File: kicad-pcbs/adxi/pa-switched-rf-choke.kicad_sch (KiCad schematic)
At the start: 51 parts

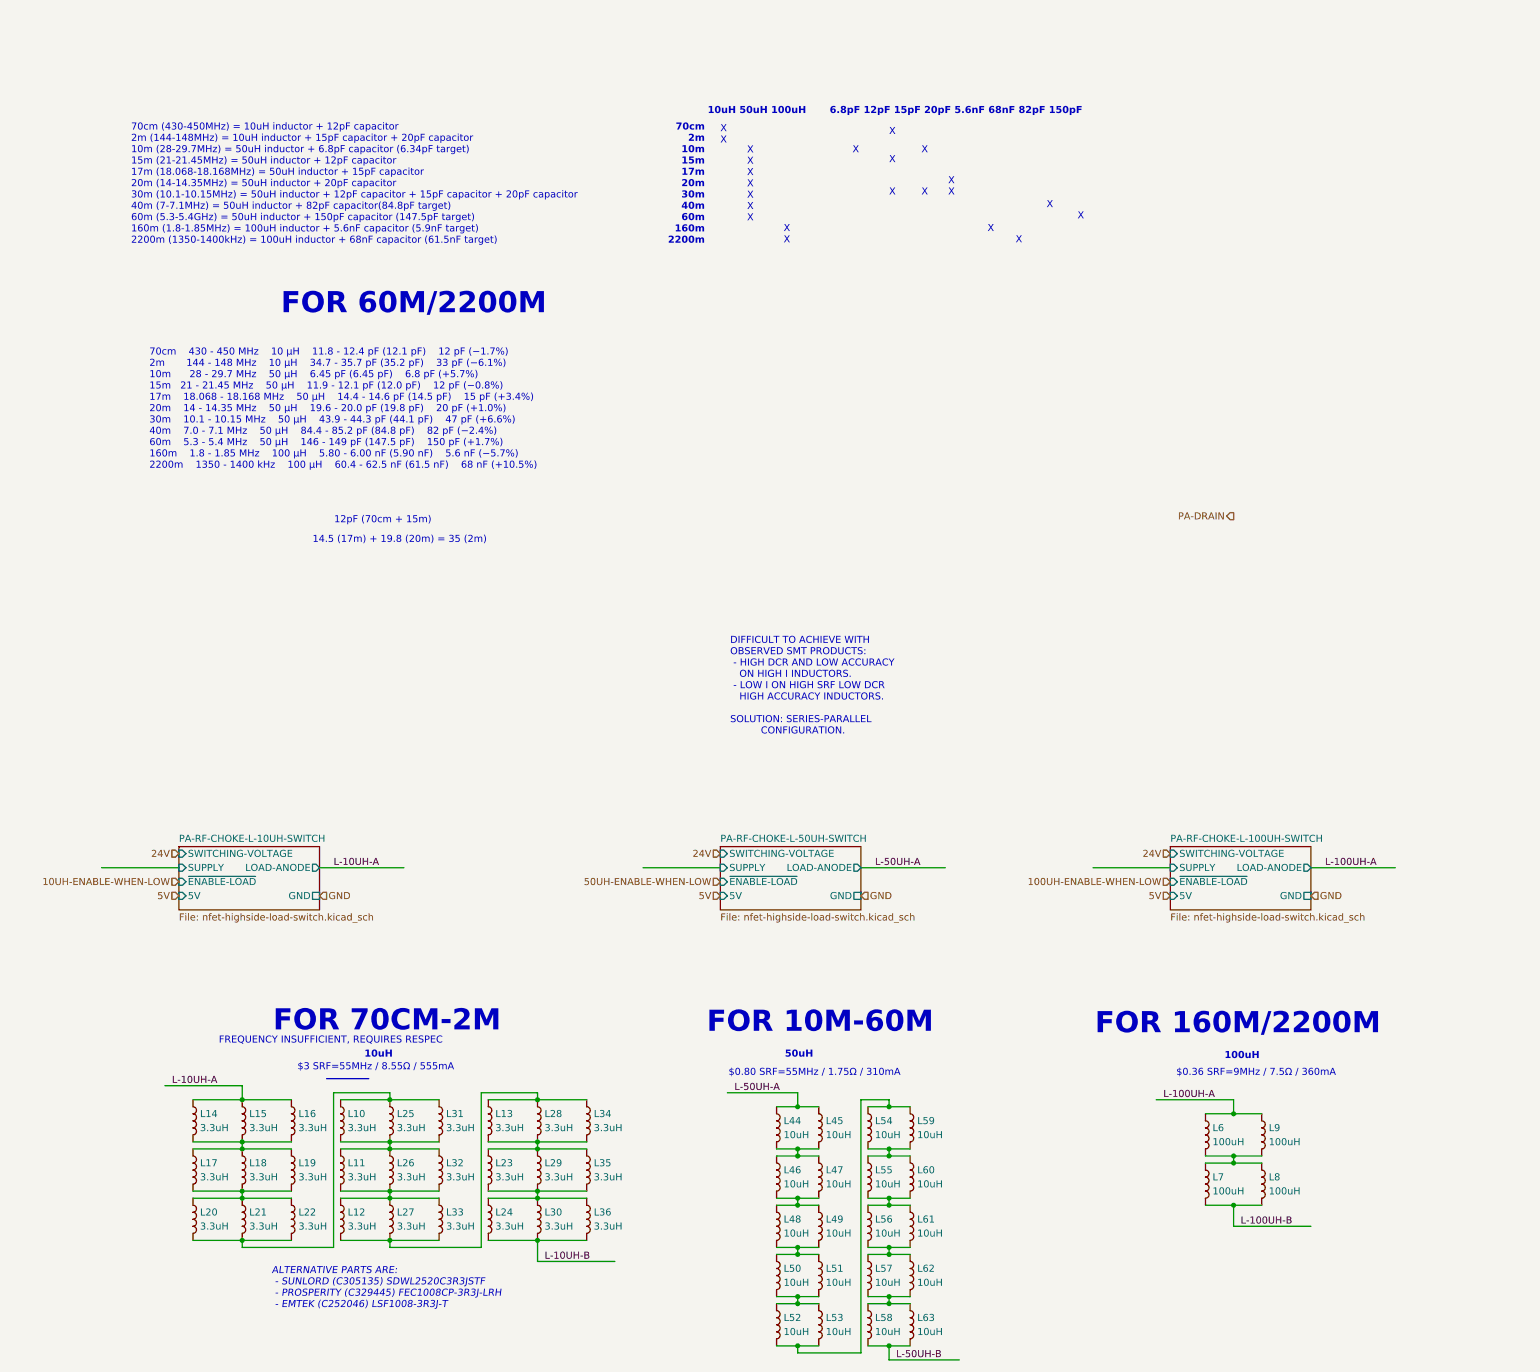
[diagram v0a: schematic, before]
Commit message: Working inductor array
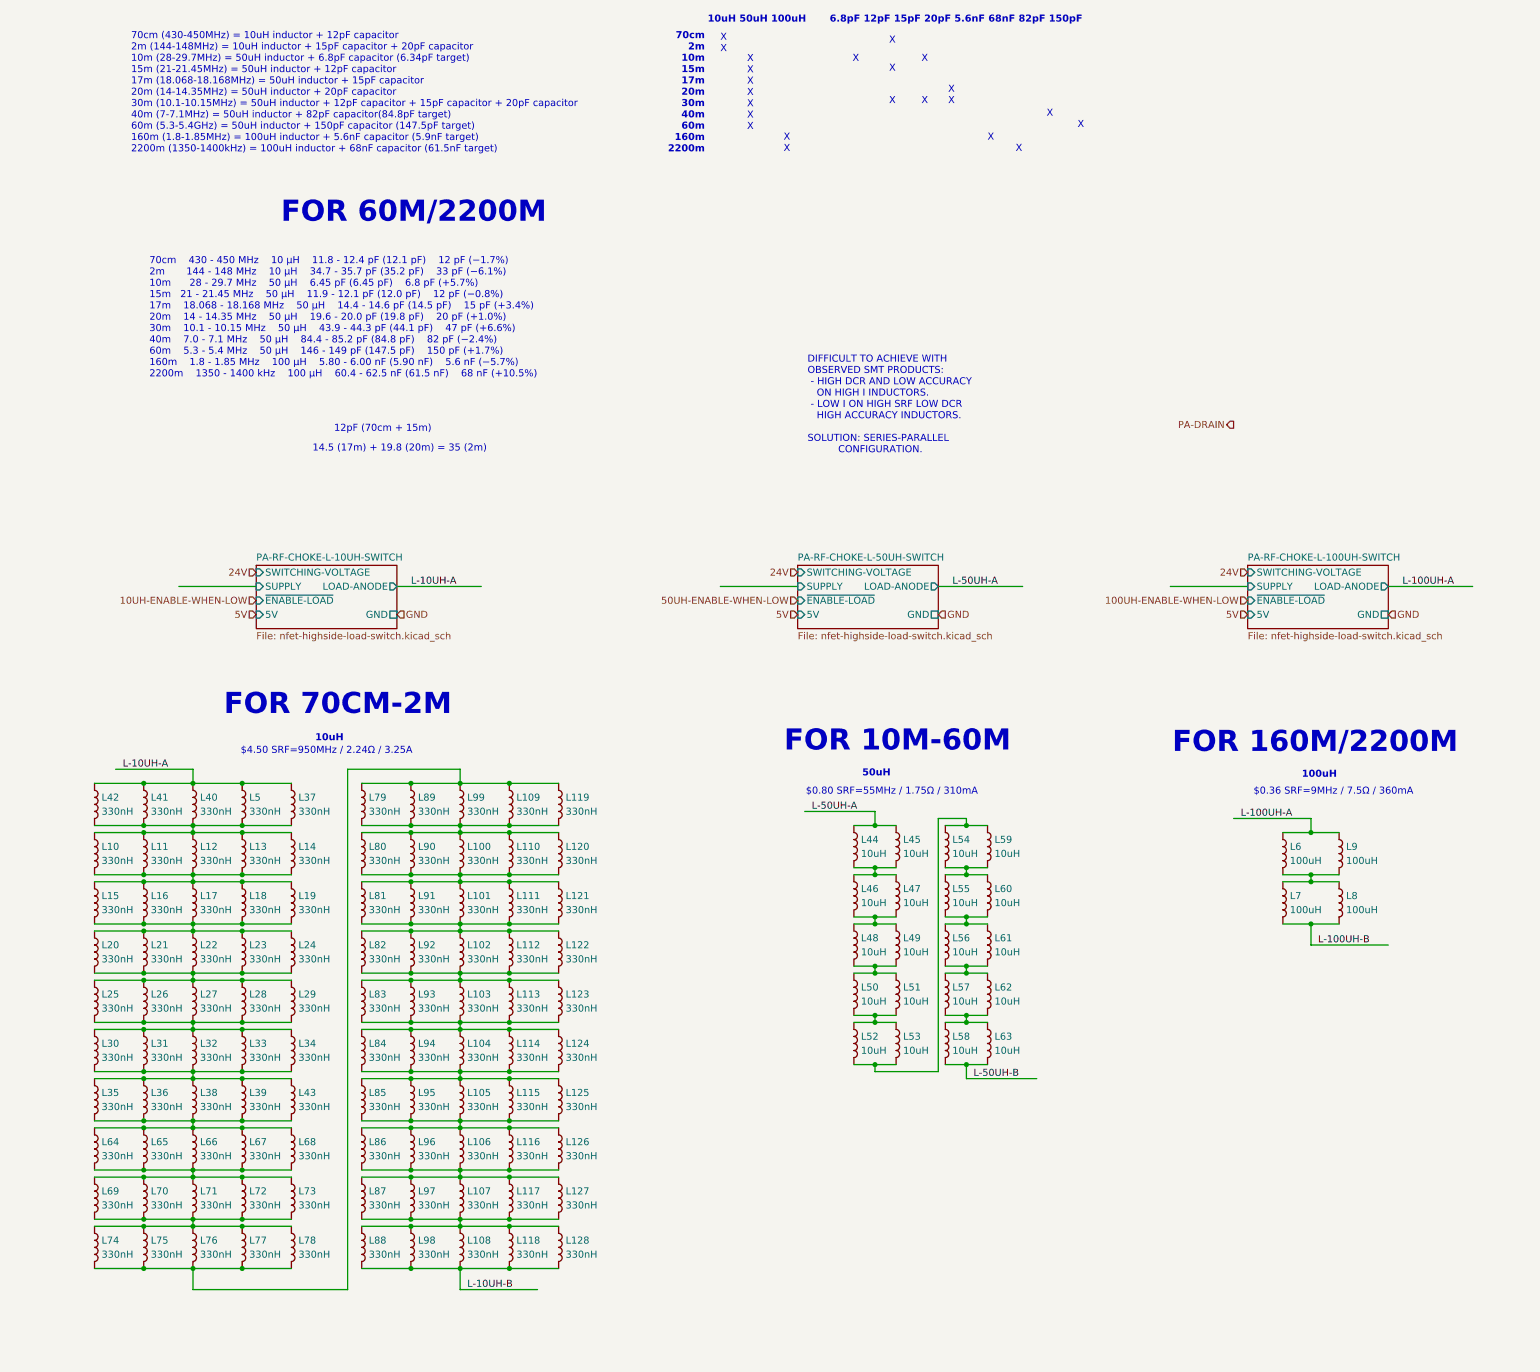
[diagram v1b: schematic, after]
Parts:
- added L100, L101, L102, L103, L104, L105, L106, L107, L108, L109, L110, L111, L112, L113, L114, L115, L116, L117, L118, L119, L120, L121, L122, L123, L124, L125, L126, L127, L128, L37, L38, L39, L40, L41, L42, L43, L5, L64, L65, L66, L67, L68, L69, L70, L71, L72, L73, L74, L75, L76, L77, L78, L79, L80, L81, L82, L83, L84, L85, L86, L87, L88, L89, L90, L91, L92, L93, L94, L95, L96, L97, L98, L99: 330nH, Inductor_SMD:L_1008_2520Metric, symbol Device:L
- L10, L11, L12, L13, L14, L15, L16, L17, L18, L19, L20, L21, L22, L23, L24, L25, L26, L27, L28, L29, L30, L31, L32, L33, L34, L35, L36: value 3.3uH -> 330nH; LCSC Part # C295353 -> C346437; MPN NLV25T-3R3J-EFD -> FEC1008CP-R10; Manufacturer TDK -> Prosperity
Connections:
- net L-10UH-A: now also L37.1, L40.1, L41.1, L42.1, L5.1; no longer L14.1, L15.1, L16.1
- net L-10UH-B: now also L108.2, L118.2, L128.2, L88.2, L98.2; no longer L24.2, L30.2, L36.2
- net at L20.2, L21.2, L22.2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: now also L23.2, L24.2, L26.1, L27.1, L28.1, L29.1; no longer L10.1, L31.1
- net at L14.2, L17.1, L18.1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: now also L10.2, L11.2, L12.2, L13.2, L15.1, L16.1; no longer L15.2, L16.2
- net at L17.2, L18.2, L19.2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: now also L15.2, L16.2, L23.1, L24.1
- new net: L25.2, L26.2, L27.2, L28.2, L29.2, L30.1, L31.1, L32.1, L33.1, L34.1
- new net: L10.1, L11.1, L12.1, L13.1, L14.1, L37.2, L40.2, L41.2, L42.2, L5.2
- new net: L102.2, L103.1, L112.2, L113.1, L122.2, L123.1, L82.2, L83.1, L92.2, L93.1
- new net: L103.2, L104.1, L113.2, L114.1, L123.2, L124.1, L83.2, L84.1, L93.2, L94.1
- new net: L109.1, L119.1, L74.2, L75.2, L76.2, L77.2, L78.2, L79.1, L89.1, L99.1
- new net: L100.1, L109.2, L110.1, L119.2, L120.1, L79.2, L80.1, L89.2, L90.1, L99.2
- new net: L30.2, L31.2, L32.2, L33.2, L34.2, L35.1, L36.1, L38.1, L39.1, L43.1
- new net: L35.2, L36.2, L38.2, L39.2, L43.2, L64.1, L65.1, L66.1, L67.1, L68.1
- new net: L104.2, L105.1, L114.2, L115.1, L124.2, L125.1, L84.2, L85.1, L94.2, L95.1
- new net: L100.2, L101.1, L110.2, L111.1, L120.2, L121.1, L80.2, L81.1, L90.2, L91.1
- new net: L101.2, L102.1, L111.2, L112.1, L121.2, L122.1, L81.2, L82.1, L91.2, L92.1
- new net: L105.2, L106.1, L115.2, L116.1, L125.2, L126.1, L85.2, L86.1, L95.2, L96.1
- new net: L64.2, L65.2, L66.2, L67.2, L68.2, L69.1, L70.1, L71.1, L72.1, L73.1
- new net: L69.2, L70.2, L71.2, L72.2, L73.2, L74.1, L75.1, L76.1, L77.1, L78.1
- new net: L106.2, L107.1, L116.2, L117.1, L126.2, L127.1, L86.2, L87.1, L96.2, L97.1
- new net: L107.2, L108.1, L117.2, L118.1, L127.2, L128.1, L87.2, L88.1, L97.2, L98.1
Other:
- note added: "$4.50 SRF=950MHz / 2.24Ω / 3.25A"
- note removed: "$3 SRF=55MHz / 8.55Ω / 555mA"
- note removed: "ALTERNATIVE PARTS ARE: - SUNLORD (C305135) SDWL2520C3R3JSTF - PROSPERITY (C329445) FEC1008CP-3R3J-LRH - EMTEK (C252046) LSF1008-3R3J-T"
- note removed: "FREQUENCY INSUFFICIENT, REQUIRES RESPEC"
- moved on the sheet: L44, L45, L46, L47, L48, L49, L50, L51, L52, L53, L54, L55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
